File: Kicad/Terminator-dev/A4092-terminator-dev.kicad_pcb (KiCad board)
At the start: 2 copper layers, 72.3 x 32.3 mm, 14 parts, among them J1 Conn_02x25_Odd_Even, Q1 AO3401A, U1 LT1118-2.85

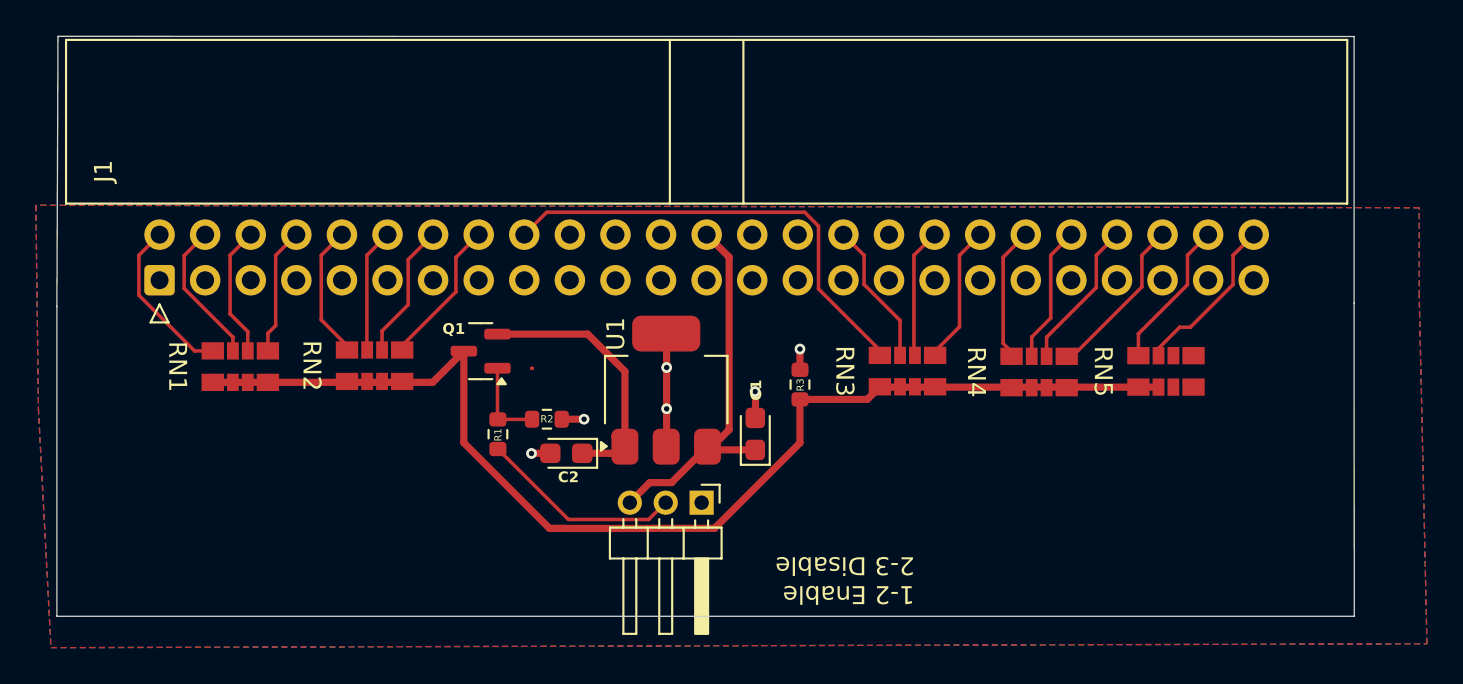
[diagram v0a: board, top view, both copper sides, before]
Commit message: Update DEV version of the terminator
with switch for experimenting w/ mosfet
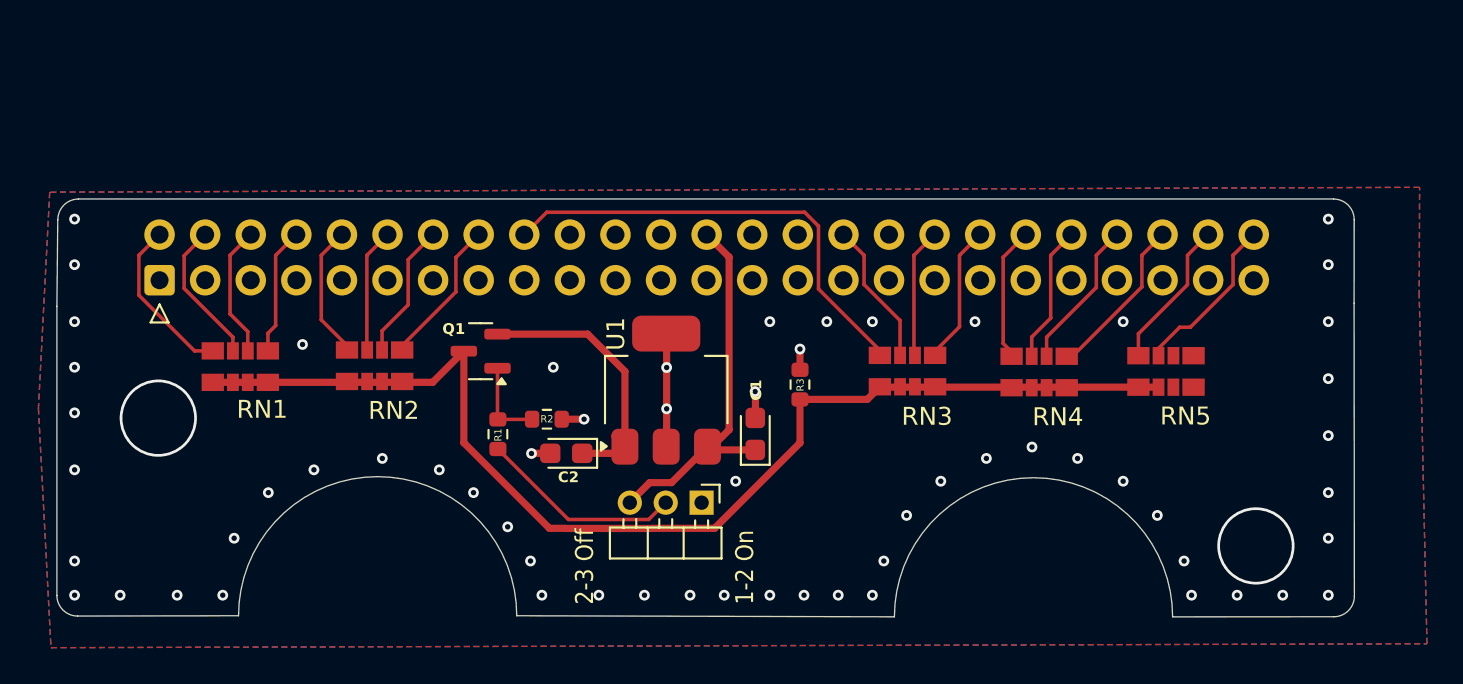
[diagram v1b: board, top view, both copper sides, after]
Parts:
- J1: footprint Connector_IDC:IDC-Header_2x25_P2.54mm_Horizontal -> Connector_IDC_local:IDC-Header_2x25_P2.54mm_Horizontal
- JP1: value 1-2 Enable 2-3 Disable -> 1-2 Enable; 2-3 Disable
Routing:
- net GND: vias 6 -> 62
- net (no net): vias 0 -> 2
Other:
- board size 72.3 x 32.3 mm -> 72.3 x 23.3 mm
- board text added: "1-2 On"
- board text added: "2-3 Off"
- board text added: "A4092"
- board text added: "PROTO A"
- board text removed: "1-2 Enable 2-3 Disable"
- board text removed: "•"
